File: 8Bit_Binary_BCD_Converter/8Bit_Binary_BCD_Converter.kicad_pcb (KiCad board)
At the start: 4 copper layers, 32 x 52 mm, 30 parts, among them U1 74HC283, U10 74HC283, U11 74LVC2G32, U12 SN74LVC1G08DCKR, U13 74HC283, U14 74LVC2G32, U15 SN74LVC1G08DCKR, U16 74HC283, U17 74LVC2G32, U18 SN74LVC1G08DCKR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

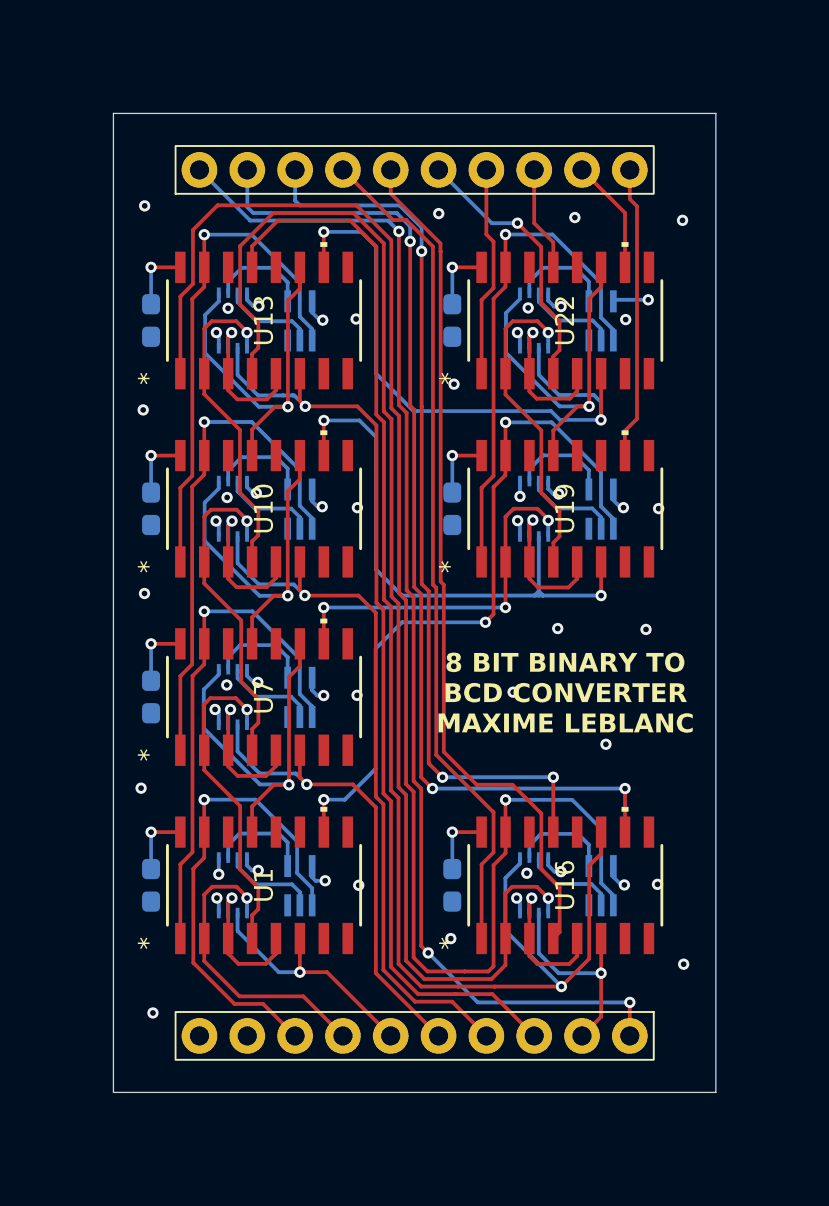
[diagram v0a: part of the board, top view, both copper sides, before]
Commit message: Finished BCD Converter + BOM + Gerber Files
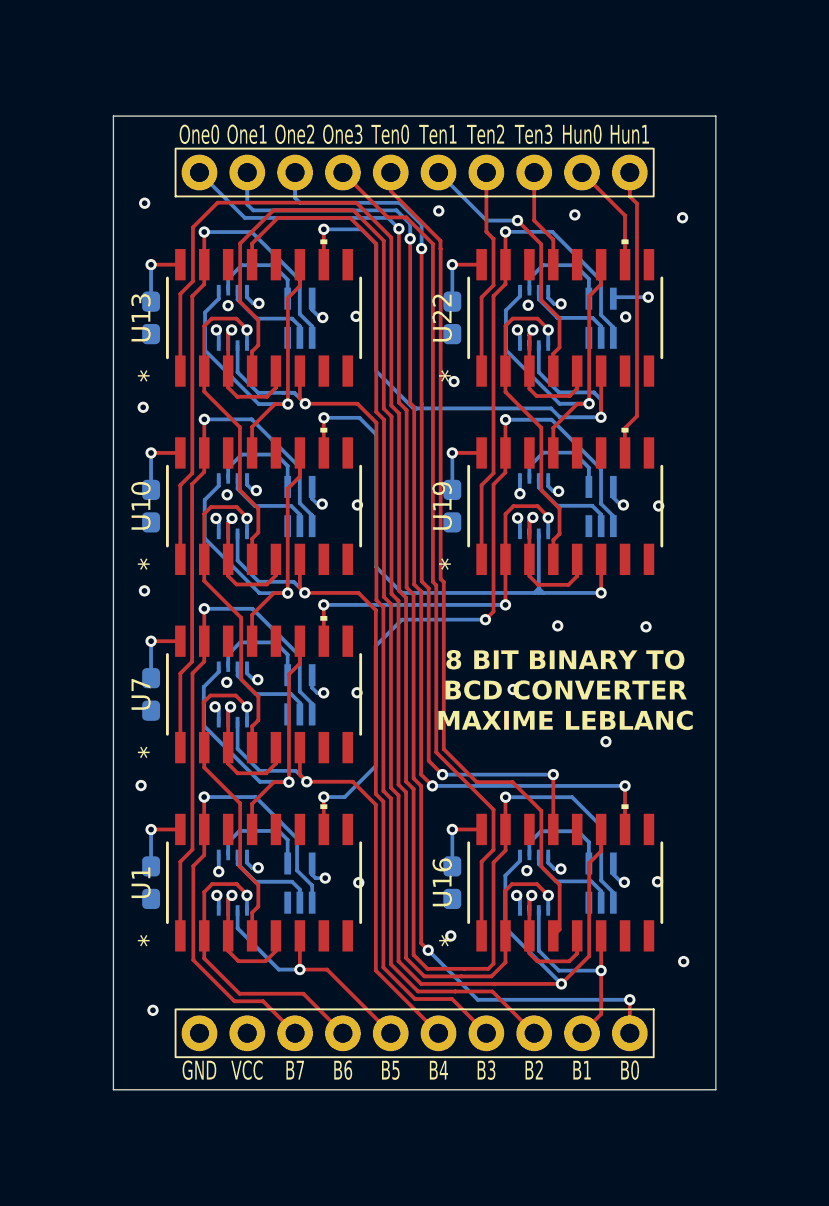
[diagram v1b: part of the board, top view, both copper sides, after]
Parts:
- moved C1 0.14 mm to (136.0, 123.9)
- moved C2 0.14 mm to (136.0, 113.9)
- moved C3 0.14 mm to (136.0, 103.9)
- moved C4 0.14 mm to (136.0, 93.9)
- moved C5 0.14 mm to (152.0, 123.9)
- moved C6 0.14 mm to (152.0, 103.9)
- moved C7 0.14 mm to (152.0, 93.9)
- moved U1 0.14 mm to (142.0, 123.9)
- moved U10 0.14 mm to (142.0, 103.9)
- moved U11 0.14 mm to (140.3, 93.9)
- moved U12 0.14 mm to (143.9, 93.9)
- moved U13 0.14 mm to (142.0, 93.9)
- moved U14 0.14 mm to (156.3, 123.9)
- moved U15 0.14 mm to (159.9, 123.9)
- moved U16 0.14 mm to (158.0, 123.9)
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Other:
- board size 32 x 52 mm -> 32 x 51.7 mm
- board text added: "B0"
- board text added: "B1"
- board text added: "B2"
- board text added: "B3"
- board text added: "B4"
- board text added: "B5"
- board text added: "B6"
- board text added: "B7"
- board text added: "GND"
- board text added: "Hun0"
- board text added: "Hun1"
- board text added: "One0"
- board text added: "One1"
- board text added: "One2"
- board text added: "One3"
- board text added: "Ten0"
- board text added: "Ten1"
- board text added: "Ten2"
- board text added: "Ten3"
- board text added: "VCC"

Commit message: BCD converter fix
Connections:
- U16 pad 1: Ones3 -> Ones2
- U16 pad 10: Ones1 -> Tens0
- U16 pad 13: Ones2 -> Ones3
- U16 pad 4: Tens0 -> Ones1
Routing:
- net Ones1: track 53.7 -> 56.7 mm
- net Ones3: track 44.7 -> 42.0 mm
- net Tens0: track 45.5 -> 43.9 mm
- net Ones2: track 47.1 -> 48.6 mm, vias 3 -> 1
- net GND: vias 36 -> 37
